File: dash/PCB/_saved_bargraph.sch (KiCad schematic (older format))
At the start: 100 parts, among them IC1 ATMEGA328-P, J1 DB9, P1 USB_OTG, P2 CONN_02X05, P3 CONN_02X05, P4 CONN_02X05, P5 CONN_02X05, Q1 BC557, Q2 BC547, U1 CH340G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

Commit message: One of the boards completed at least
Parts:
- removed AFF1: LTS-6980HR, addlol:7seg, symbol LTS-6980HR
- added AFF?: 7SEGMENTS, symbol 7SEGMENTS
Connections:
- net 12Vraw: no longer P4.3 (P3), P4.4 (P4), P5.3 (P3), P5.4 (P4)
- net 12vraw: now also P4.3 (P3), P4.4 (P4), P5.3 (P3), P5.4 (P4)
- net Vcc: now also AFF?.3 (C.A.), AFF?.8 (C.A.)
- net at R43.1: now also AFF?.1 (e)
- net at R46.1: now also AFF?.10 (g)
- net at R42.1: now also AFF?.2 (d)
- net at R41.1: now also AFF?.4 (c)
- net at R47.1: now also AFF?.5 (DP)
- net at R39.1: now also AFF?.6 (b)
- net at R37.1: now also AFF?.7 (a)
- net at R44.1: now also AFF?.9 (f)
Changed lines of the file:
@@
 Vcc
-$Comp
-L LTS-6980HR AFF1
-U 1 1 572FFC5A
-P 2800 7000
-F 0 "AFF1" H 2800 7550 50  0000 C CNN
-F 1 "LTS-6980HR" H 2800 6550 50  0000 C CNN
-F 2 "addlol:7seg" H 2800 7000 50  0001 C CNN
-F 3 "" H 2800 7000 50  0000 C CNN
-	1    2800 7000
-	1    0    0    -1
-$EndComp
 $Comp
 L R R37
@@
 	1    2050 7300
 	0    1    1    0
-$EndComp
-$Comp
-L GNDREF #PWR37
-U 1 1 57300AE0
-P 3400 6650
-F 0 "#PWR37" H 3400 6400 50  0001 C CNN
-F 1 "GNDREF" H 3400 6500 50  0000 C CNN
-F 2 "" H 3400 6650 50  0000 C CNN
-F 3 "" H 3400 6650 50  0000 C CNN
-	1    3400 6650
-	1    0    0    -1
 $EndComp
 Text Label 1100 6700 2    60   ~ 0
@@
 $EndComp
 Text Label 12850 4900 2    60   ~ 0
-12Vraw
+12vraw
 Text Label 13350 4900 0    60   ~ 0
-12Vraw
+12vraw
 Text Label 13800 4900 2    60   ~ 0
-12Vraw
+12vraw
 Text Label 14300 4900 0    60   ~ 0
-12Vraw
+12vraw
 Text Label 5200 6850 3    60   ~ 0
 intShiftLight
@@
 Text Label 14300 5000 0    60   ~ 0
 intShiftLight
+$Comp
+L 7SEGMENTS AFF?
+U 1 1 5736B60E
+P 2800 7000
+F 0 "AFF?" H 2800 7675 50  0000 C CNN
+F 1 "7SEGMENTS" H 2800 7584 50  0000 C CNN
+F 2 "" H 2800 7000 50  0000 C CNN
+F 3 "" H 2800 7000 50  0000 C CNN
+	1    2800 7000
+	1    0    0    -1
+$EndComp
+Text Label 3400 6550 0    60   ~ 0
+Vcc
 $EndSCHEMATC

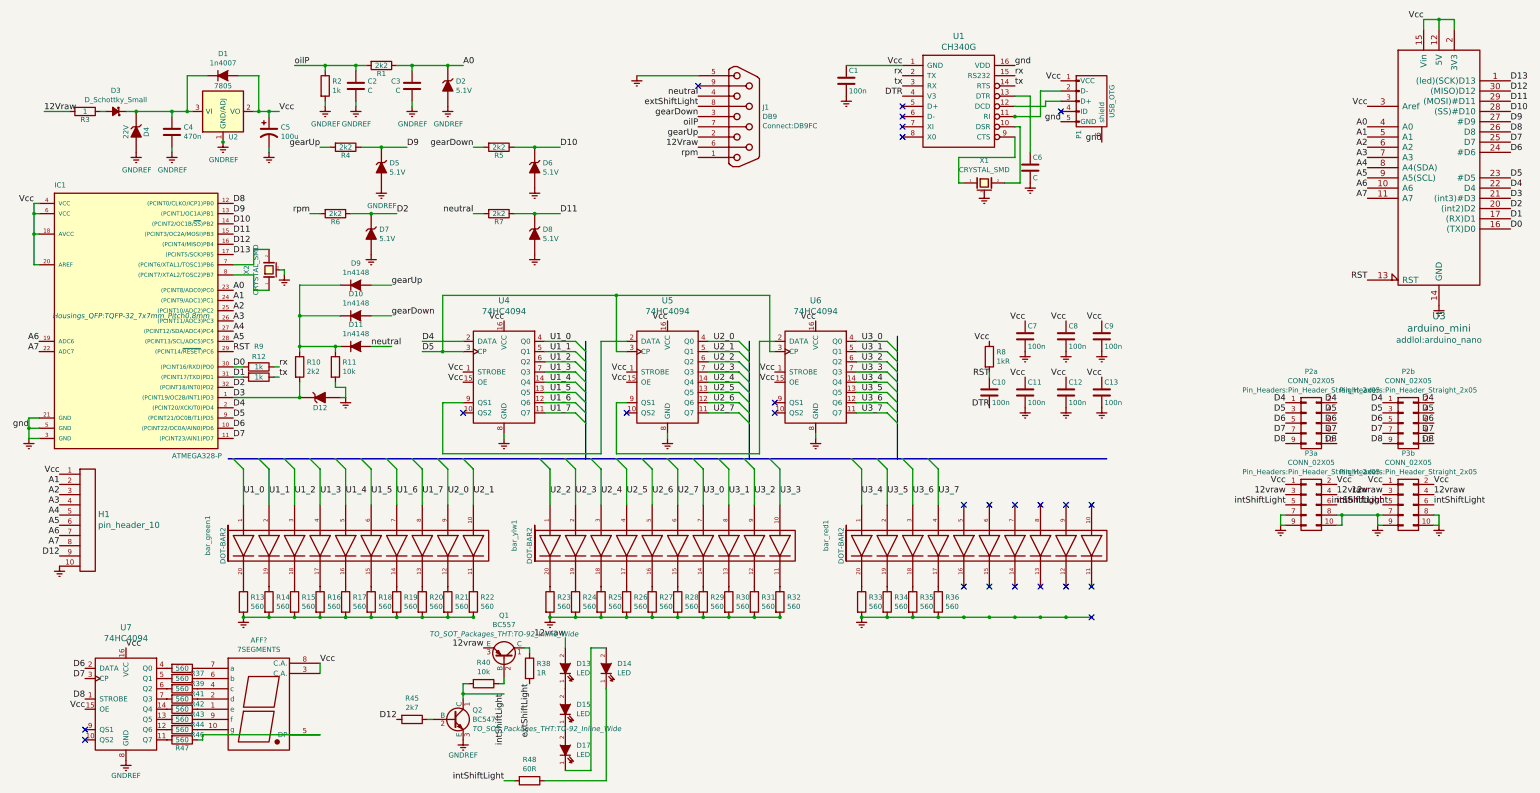
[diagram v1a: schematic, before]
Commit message: Fixing bugs in the PCB designe
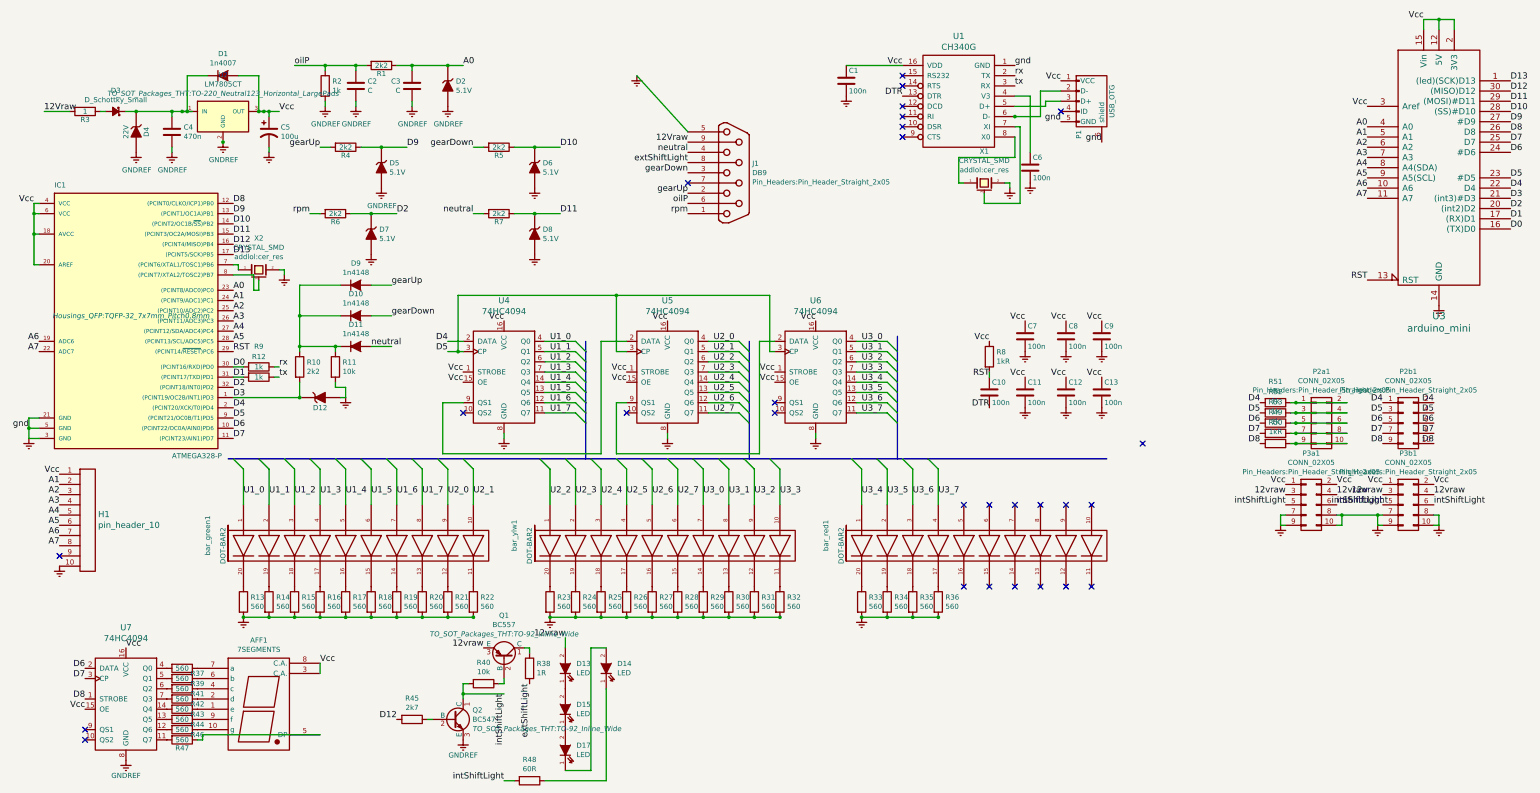
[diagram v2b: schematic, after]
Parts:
- removed U2: 7805, TO_SOT_Packages_THT:TO-220_Neutral123_Horizontal, symbol AP1117
- added R49, R52, R53: 1k, Resistors_SMD:R_0805_HandSoldering, symbol R
- added R50: 1kR, Resistors_SMD:R_0805_HandSoldering, symbol R
- added R51: R, Resistors_SMD:R_0805_HandSoldering, symbol R
- added U2: LM7805CT, TO_SOT_Packages_THT:TO-220_Neutral123_Horizontal_LargePads, symbol LM7805CT
- AFF1: renamed from AFF?; footprint (none) -> addlol:7seg
- C6: value C -> 100n
- J1: footprint Connect:DB9FC -> Pin_Headers:Pin_Header_Straight_2x05
- U3: footprint addlol:arduino_nano -> (none)
- renumbered P2 to P2a1, P3 to P2b1, P4 to P3a1, P5 to P3b1
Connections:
- net 12Vraw: now also J1.9 (P9); no longer J1.6 (P6)
- net D12: no longer H1.9
- net D4: now also R51.2; no longer P2a1.1 (P1), P2a1.2 (P2)
- net D5: now also R52.2; no longer P2a1.3 (P3), P2a1.4 (P4)
- net D6: now also R53.2; no longer P2a1.5 (P5), P2a1.6 (P6)
- net D7: now also R49.2; no longer P2a1.7 (P7), P2a1.8 (P8)
- net D8: now also R50.2; no longer P2a1.10 (P10), P2a1.9 (P9)
- net DTR: now also U1.13 (DTR); no longer U1.4 (V3)
- net GNDREF: now also U1.1 (GND), X1.2, X2.2, U2.2 (GND); no longer U1.16 (VDD), X1.3 (case), X2.3 (case)
- net Vcc: now also U1.16 (VDD), U2.3 (OUT); no longer U1.1 (GND)
- net oilP: now also J1.6 (P6); no longer J1.7 (P7)
- net rx: no longer U1.15 (RS232)
- net tx: no longer U1.14 (RTS)
- net at C4.1, D1.1 (K), D3.1 (K)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: now also U2.1 (IN)
- net at IC1.7 ((PCINT6/XTAL1/TOSC1)PB6): now also X2.1; no longer X2.2
- net at IC1.8 ((PCINT7/XTAL2/TOSC2)PB7): now also X2.3 (case); no longer X2.1
- net at P1.2 (D-): now also U1.6 (D-); no longer U1.11 (RI)
- net at P1.3 (D+): now also U1.5 (D+); no longer U1.12 (DCD)
- net at C6.1: now also U1.4 (V3); no longer U1.13 (DTR)
- net at X1.1: now also U1.8 (X0); no longer U1.9 (CTS)
- net at U1.10 (DSR): no longer X1.2
- net at U1.7 (XI): now also X1.3 (case)
- new net: P2a1.1 (P1), P2a1.2 (P2), R51.1
- new net: P2a1.10 (P10), P2a1.9 (P9), R50.1
- new net: P2a1.3 (P3), P2a1.4 (P4), R52.1
- new net: P2a1.5 (P5), P2a1.6 (P6), R53.1
- new net: P2a1.7 (P7), P2a1.8 (P8), R49.1
- no-connect marks 25 -> 28
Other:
- moved on the sheet: J1, P2a1
